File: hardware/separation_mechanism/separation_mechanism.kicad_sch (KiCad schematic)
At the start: 70 parts, among them IC1 74HC4052FT, J1 Conn_01x02_Socket, J3 USB_B, J4 Conn_01x02_Socket, J5 Micro_SD_Card_Det_Hirose_DM3AT, Q1 AO3400A, U1 L7805, U2 SAM-M10Q-00B, U3 SHT4x, U4 DPS368, U5 E22-900T30D_E220-900T22S(JP)_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, U6 FT4232H, U7 AP2112K-3.3, U8 93CxxB, Y1 12MHz

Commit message: feat(scm): 74HC4052 added.
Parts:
- added D5: LED, symbol Device:LED
- added IC2: 74HC4052FT, SOP65P640X120-16N, symbol Unknown:74HC4052FT
- added R23, R26: 10k, symbol Device:R_Small
- added R24, R25: 20k, symbol Device:R_Small
- added R27: 1k, symbol Device:R
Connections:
- net +3V3_MCU: now also IC2.16 (VCC)
- net FTDI_UART1_RX: now also IC1.5 (1Y), U6.17 (ADBUS1); no longer IC1.14 (1X)
- net FTDI_UART1_TX: now also IC1.14 (1X), U6.16 (ADBUS0); no longer IC1.5 (1Y)
- net GND: now also IC2.6 (INH), IC2.7 (VEE), IC2.8 (GND), IC2.9 (B), R24.2, R25.2, R27.2
- net LoRa_RXD: now also IC2.13 (X-COM)
- net LoRa_TXD: now also IC2.3 (Y-COM)
- net MCU_UART1_RX: now also IC1.1 (0Y); no longer IC1.12 (0X)
- net MCU_UART1_TX: now also IC1.12 (0X); no longer IC1.1 (0Y)
- net FTDI_UART2_TX: now reaches U6.26 (BDBUS0)
- net FTDI_UART2_TX: now also IC2.14 (1X)
- net FTDI_UART2_RX: now reaches U6.27 (BDBUS1)
- net FTDI_UART2_RX: now also IC2.5 (1Y)
- net VBUS: now reaches C10.2, J3.1 (VBUS), U7.1 (VIN)
- net VBUS: now also D5.2 (A), R23.2, R26.2
- net at IC1.10 (A): now also R23.1, R24.1
- net GNSS_STAT. renamed GNSS_STAT
- new net: D5.1 (K), R27.1
- new net: IC2.10 (A), R25.1, R26.1
- new net MCU_UART2_RX: IC2.1 (0Y)
- new net MCU_UART2_TX: IC2.12 (0X)
- no-connect marks 14 -> 18
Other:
- note added: "MCU"
- moved on the sheet: IC1

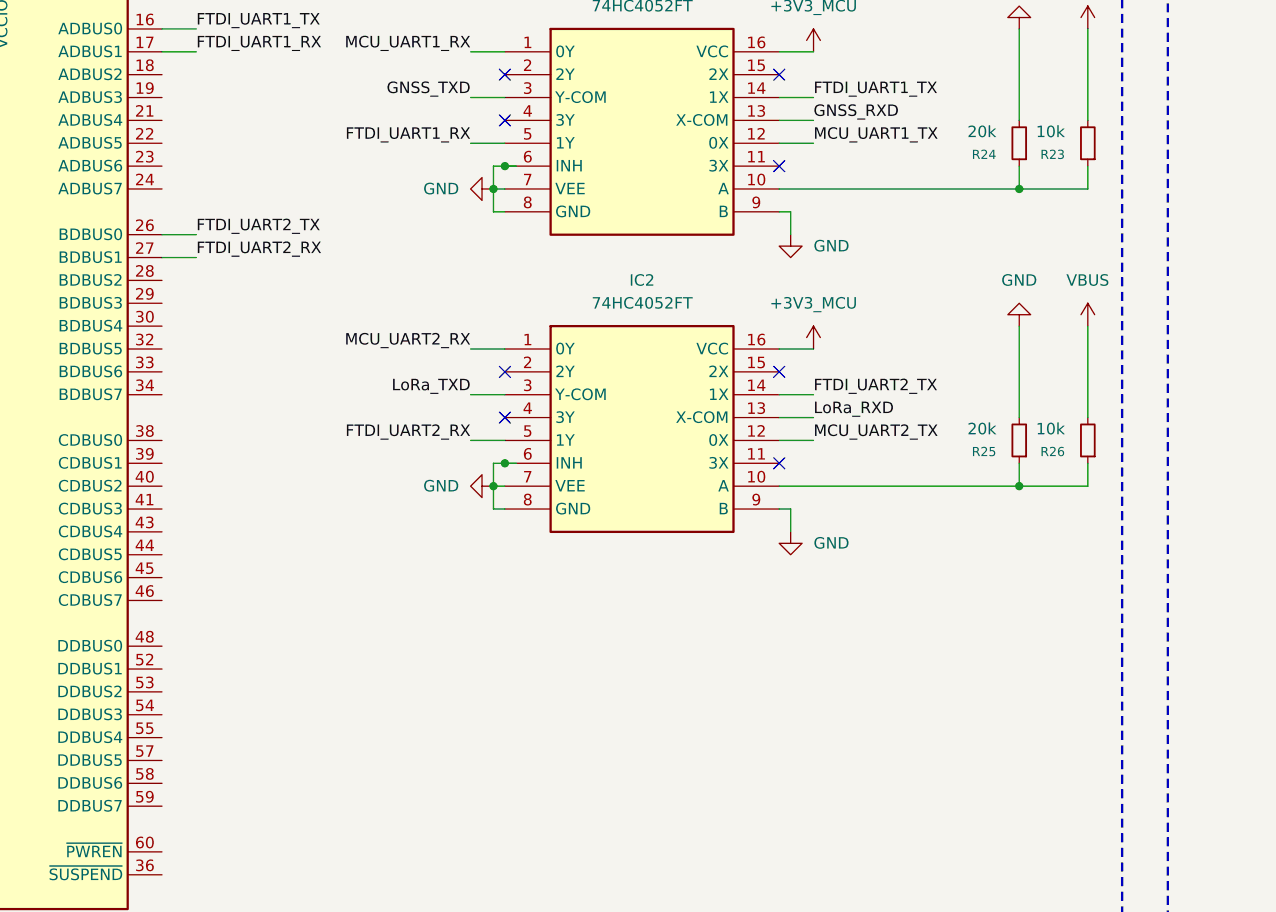
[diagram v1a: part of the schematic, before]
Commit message: fix(scm): Some text added and paper information is also configured.
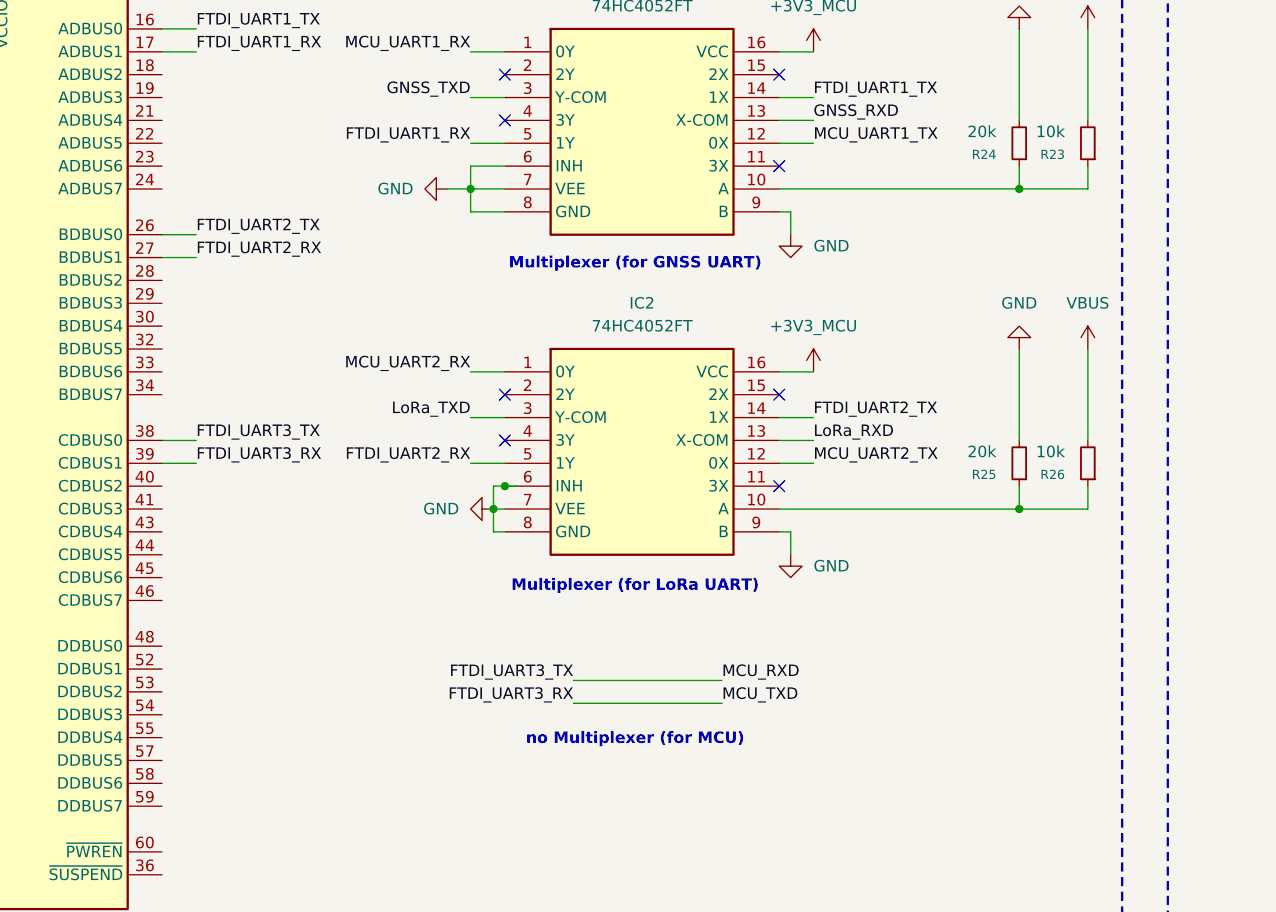
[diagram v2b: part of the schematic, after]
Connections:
- net FTDI_UART3_TX: now reaches U6.38 (CDBUS0)
- net FTDI_UART3_RX: now reaches U6.39 (CDBUS1)
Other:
- note added: "Multiplexer (for GNSS UART)"
- note added: "Multiplexer (for LoRa UART)"
- note added: "no Multiplexer (for MCU)"
- company: (none) -> Wakayama University Space Project
- title: SEPA -> 2026 MONGOLIA SEPARATION MECHANISM
- moved on the sheet: IC2, R25, R26

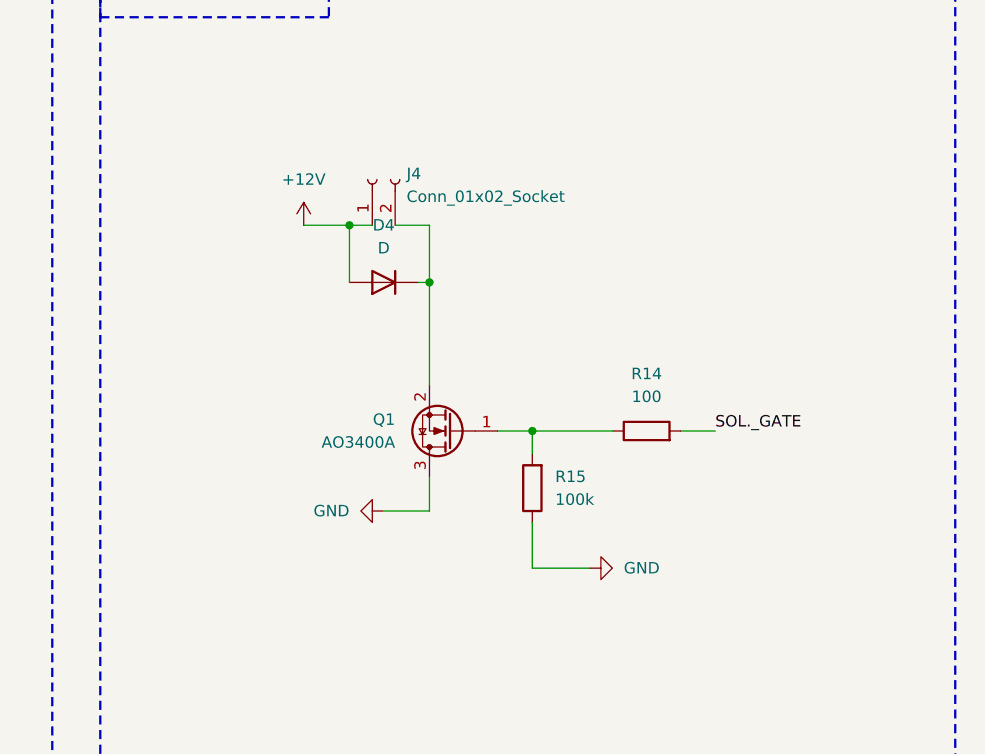
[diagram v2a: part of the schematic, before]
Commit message: fix(scm): Some parts changed their positions.
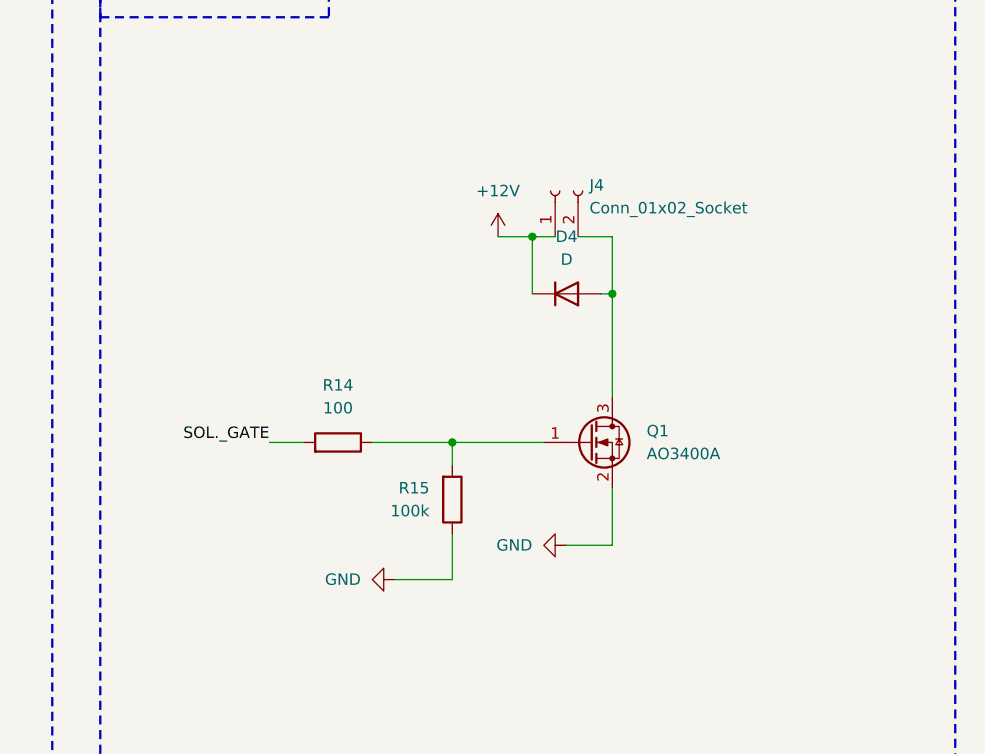
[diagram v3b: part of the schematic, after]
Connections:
- net +12V: now also D4.1 (K); no longer D4.2 (A)
- net GND: now also Q1.2 (S); no longer Q1.3 (D)
- new net: D4.2 (A), J4.2 (Pin_2), Q1.3 (D)
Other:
- moved on the sheet: D4, J4, Q1, R14, R15

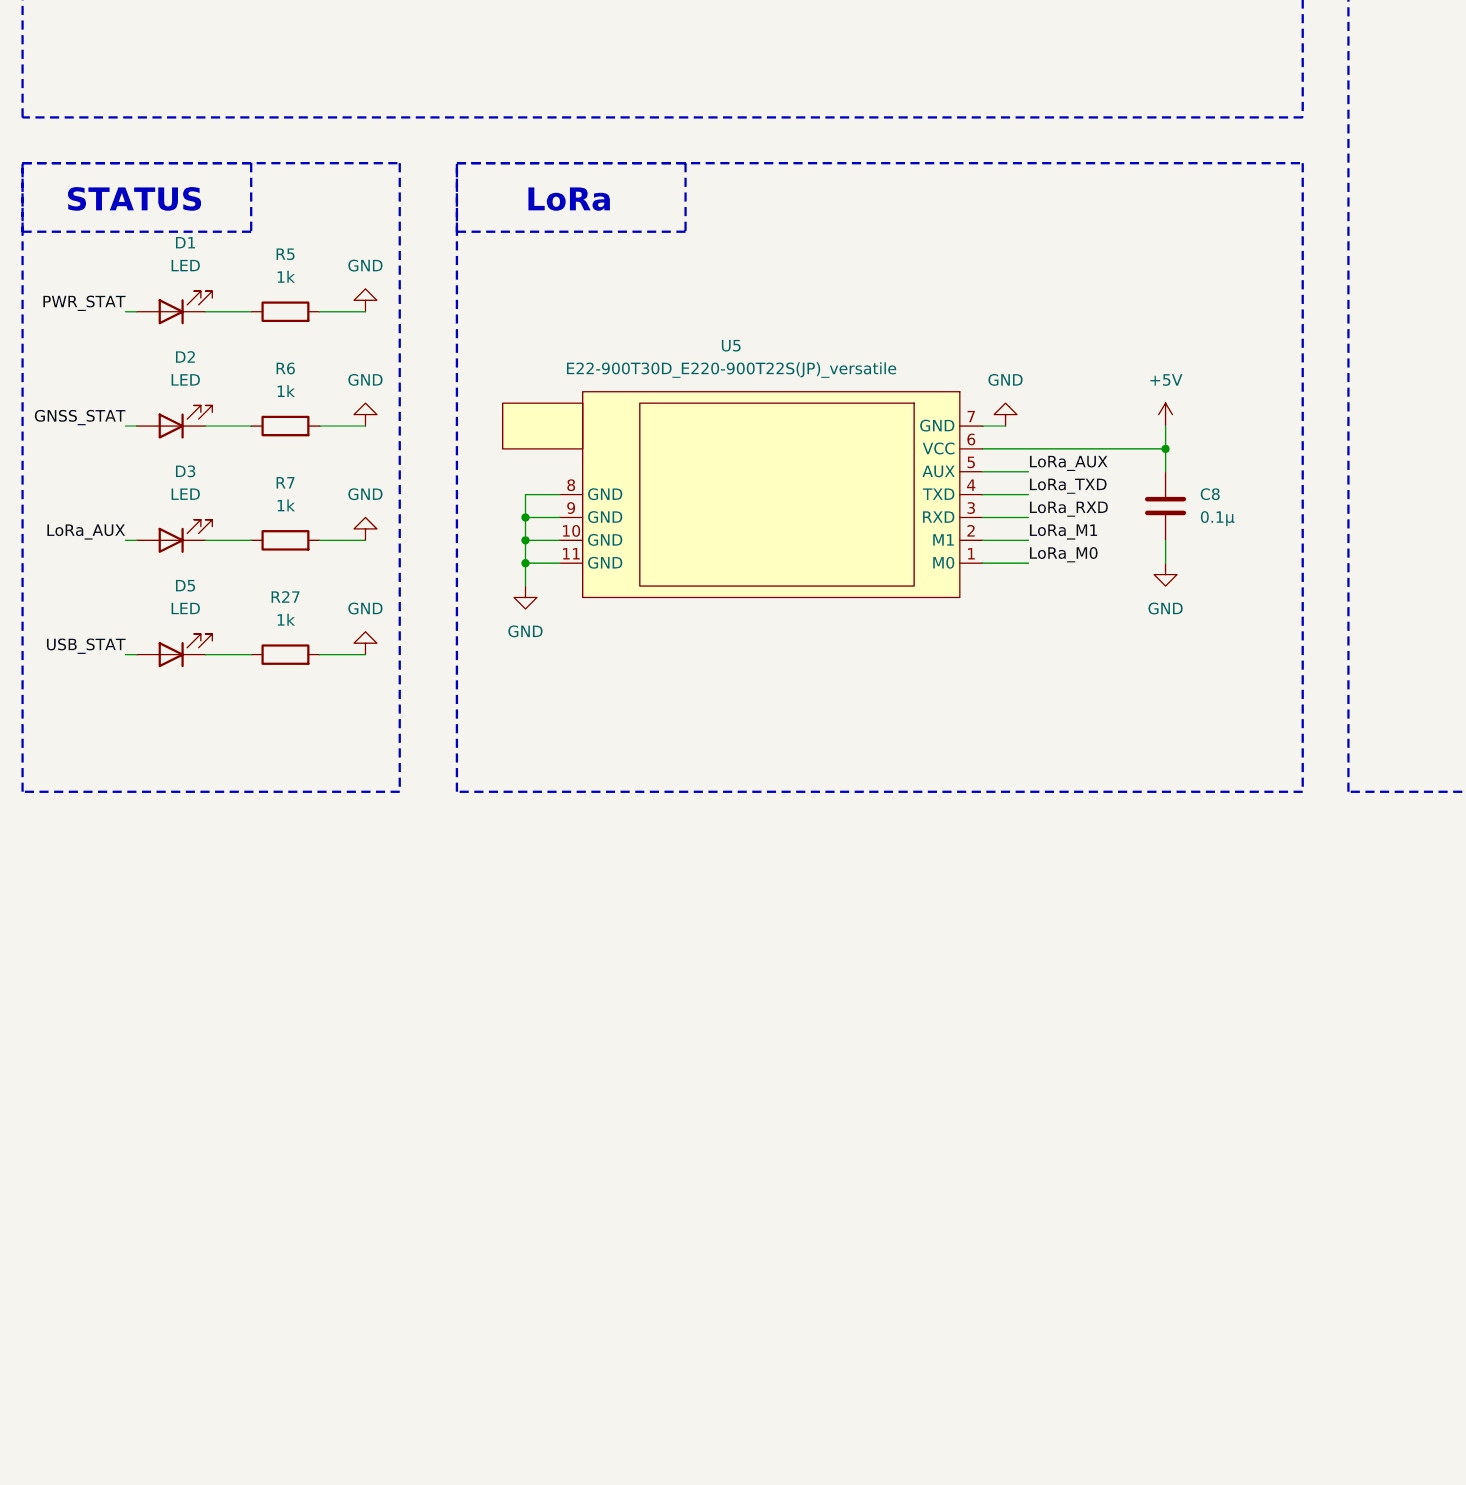
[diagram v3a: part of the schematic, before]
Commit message: feat(scm): LoRa 400MHz added.
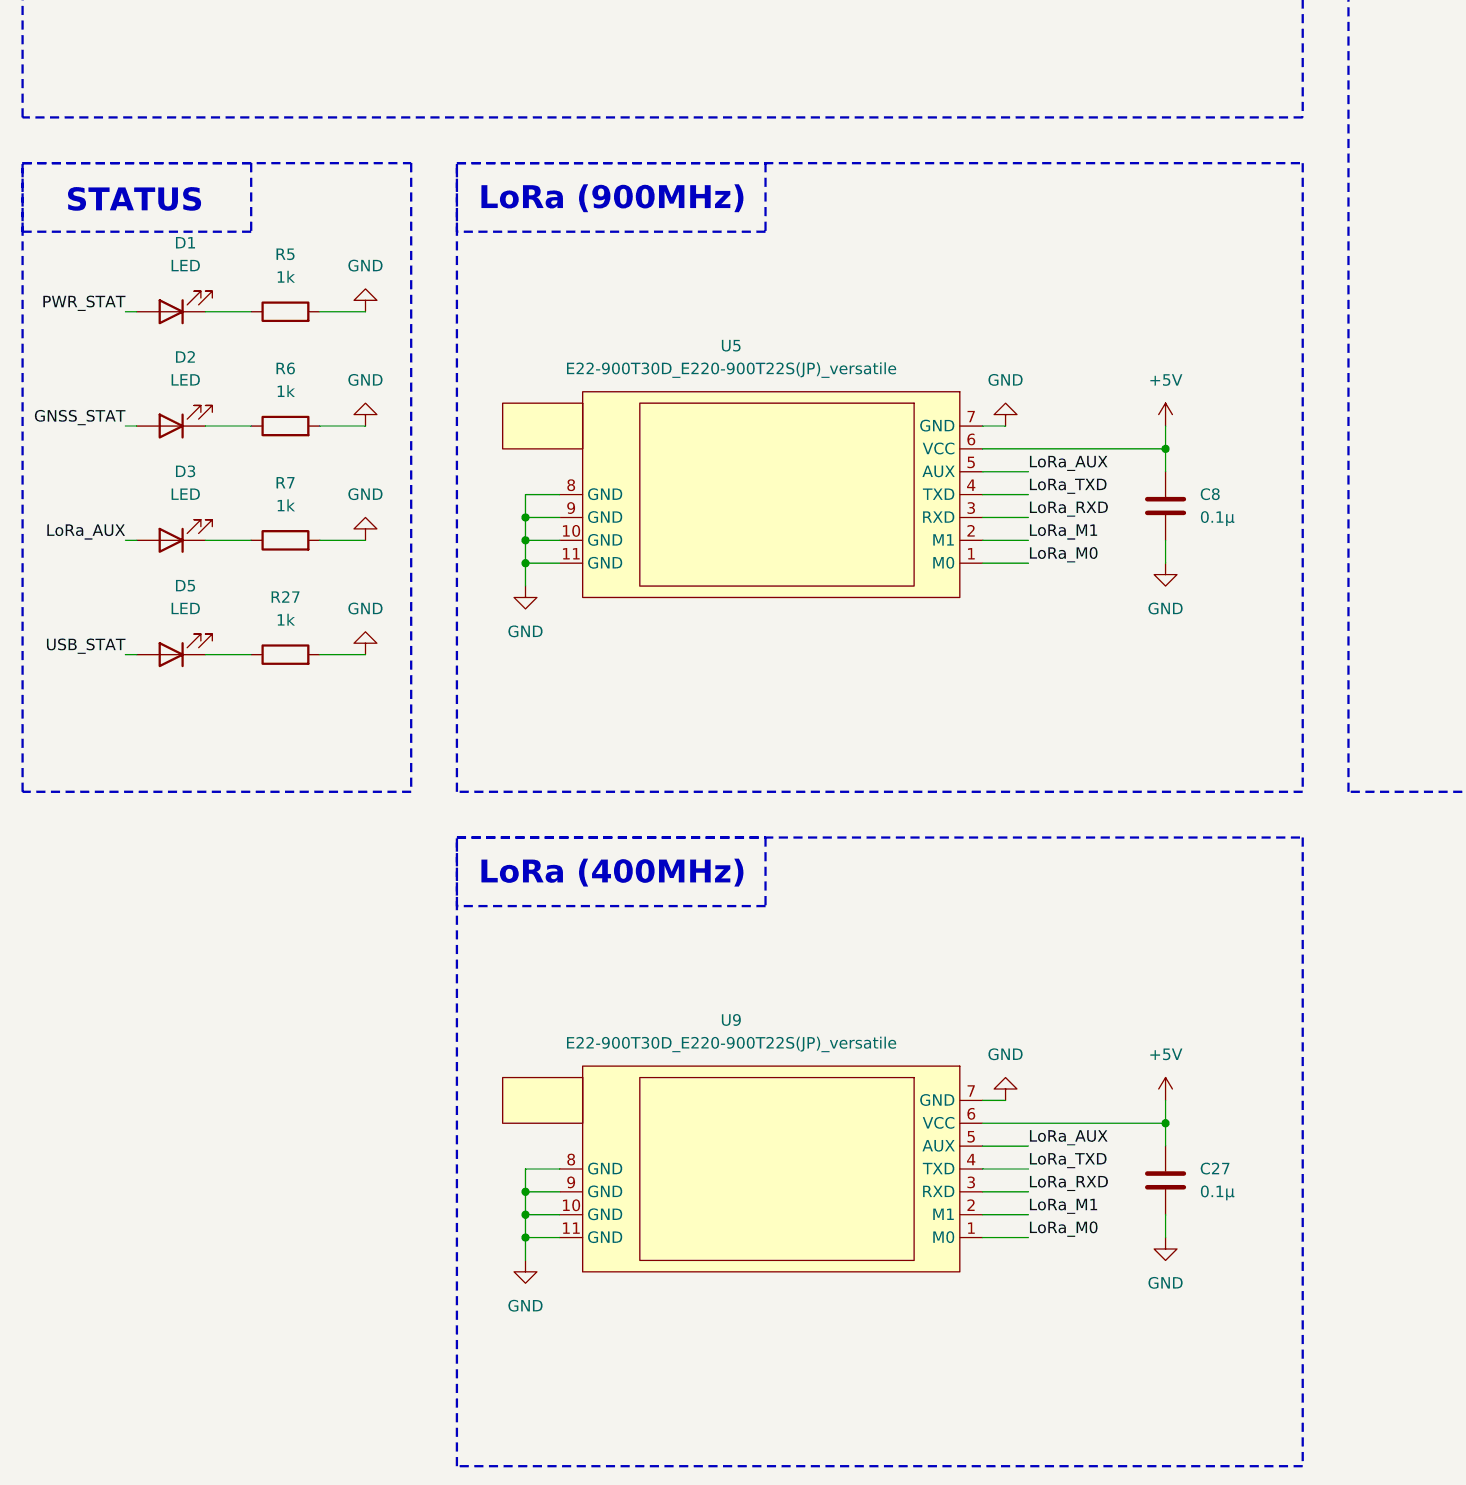
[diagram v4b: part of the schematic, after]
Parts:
- added C27: 0.1μ, symbol Device:C
- added U9: E22-900T30D_E220-900T22S(JP)_versatile, Unknown:E22-900T30D_E220-900T22S(JP)_versatile, symbol pCloud:E22-900T30D_E220-900T22S(JP)_versatile
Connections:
- net +5V: now also C27.1, U9.6 (VCC)
- net GND: now also C27.2, U9.10 (GND), U9.11 (GND), U9.7 (GND), U9.8 (GND), U9.9 (GND)
- net LoRa_AUX: now also U9.5 (AUX)
- net LoRa_M0: now also U9.1 (M0)
- net LoRa_M1: now also U9.2 (M1)
- net LoRa_RXD: now also U9.3 (RXD)
- net LoRa_TXD: now also U9.4 (TXD)
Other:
- note added: "LoRa (400MHz)"
- note added: "LoRa (900MHz)"
- note removed: "LoRa"

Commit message: feat(scm): Multiplexer added.
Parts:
- added D6: LED, symbol Device:LED
- added IC3: 74HC4052FT, SOP65P640X120-16N, symbol Unknown:74HC4052FT
- added R28: 1k, symbol Device:R
- added R29: 20k, symbol Device:R_Small
- added R30: 10k, symbol Device:R_Small
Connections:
- net +3V3_MCU: now also IC3.16 (VCC)
- net FTDI_UART3_RX: now also IC3.5 (1Y)
- net FTDI_UART3_TX: now also IC3.14 (1X)
- net GND: now also IC3.6 (INH), IC3.7 (VEE), IC3.8 (GND), IC3.9 (B), R28.2, R29.2
- net VBUS: now also R30.2
- net LoRa_AUX renamed LoRa9_AUX
- net LoRa9_AUX: no longer U9.5 (AUX)
- net LoRa_M0 renamed LoRa4_M0
- net LoRa4_M0: no longer U5.1 (M0)
- net LoRa_M1 renamed LoRa4_M1
- net LoRa4_M1: no longer U5.2 (M1)
- net LoRa_RXD renamed LoRa9_RXD
- net LoRa9_RXD: no longer U9.3 (RXD)
- net LoRa_TXD renamed LoRa9_TXD
- net LoRa9_TXD: no longer U9.4 (TXD)
- new net: D6.1 (K), R28.1
- new net: IC3.10 (A), R29.1, R30.1
- new net LoRa4_AUX: D6.2 (A), U9.5 (AUX)
- new net LoRa4_RXD: IC3.13 (X-COM), U9.3 (RXD)
- new net LoRa4_TXD: IC3.3 (Y-COM), U9.4 (TXD)
- new net LoRa9_M0: U5.1 (M0)
- new net LoRa9_M1: U5.2 (M1)
- new net MCU_UART3_RX: IC3.1 (0Y)
- new net MCU_UART3_TX: IC3.12 (0X)
- no-connect marks 18 -> 22
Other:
- note added: "Multiplexer (for LoRa 400MHz UART)"
- note added: "Multiplexer (for LoRa 900MHz UART)"
- note removed: "Multiplexer (for LoRa UART)"
- moved on the sheet: D5, R27
